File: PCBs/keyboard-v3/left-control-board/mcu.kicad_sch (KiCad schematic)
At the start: 5 parts, among them J301 F31Z1A7H111008, U301 STM32G0C1CEUx

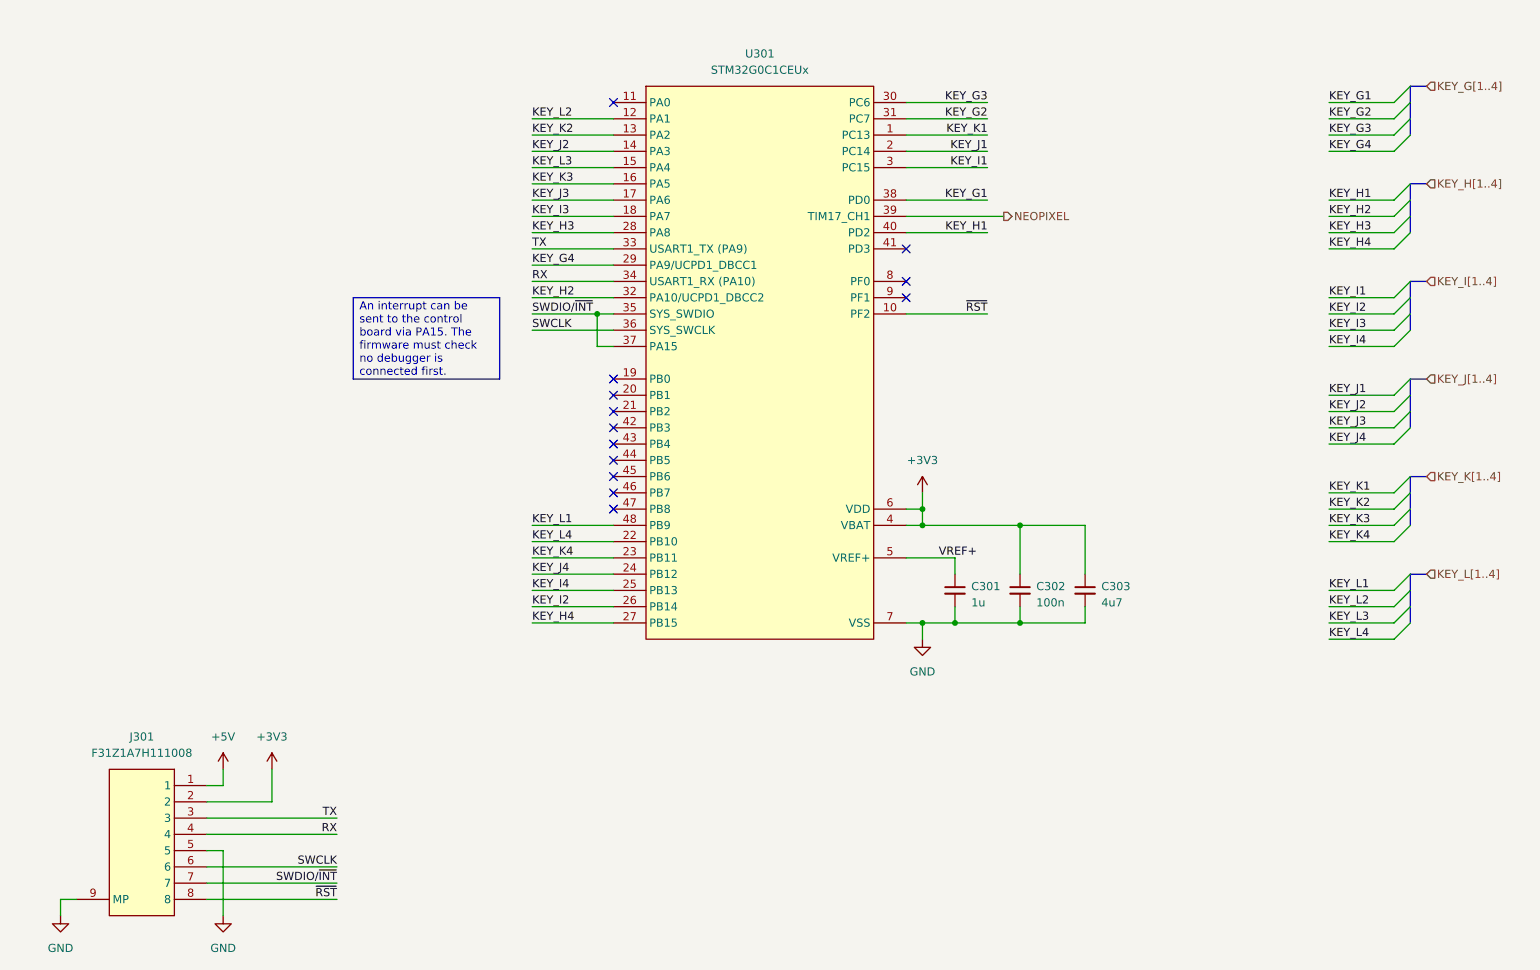
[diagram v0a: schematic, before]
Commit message: Added debug-breakout board, progress on right side schematics & layout
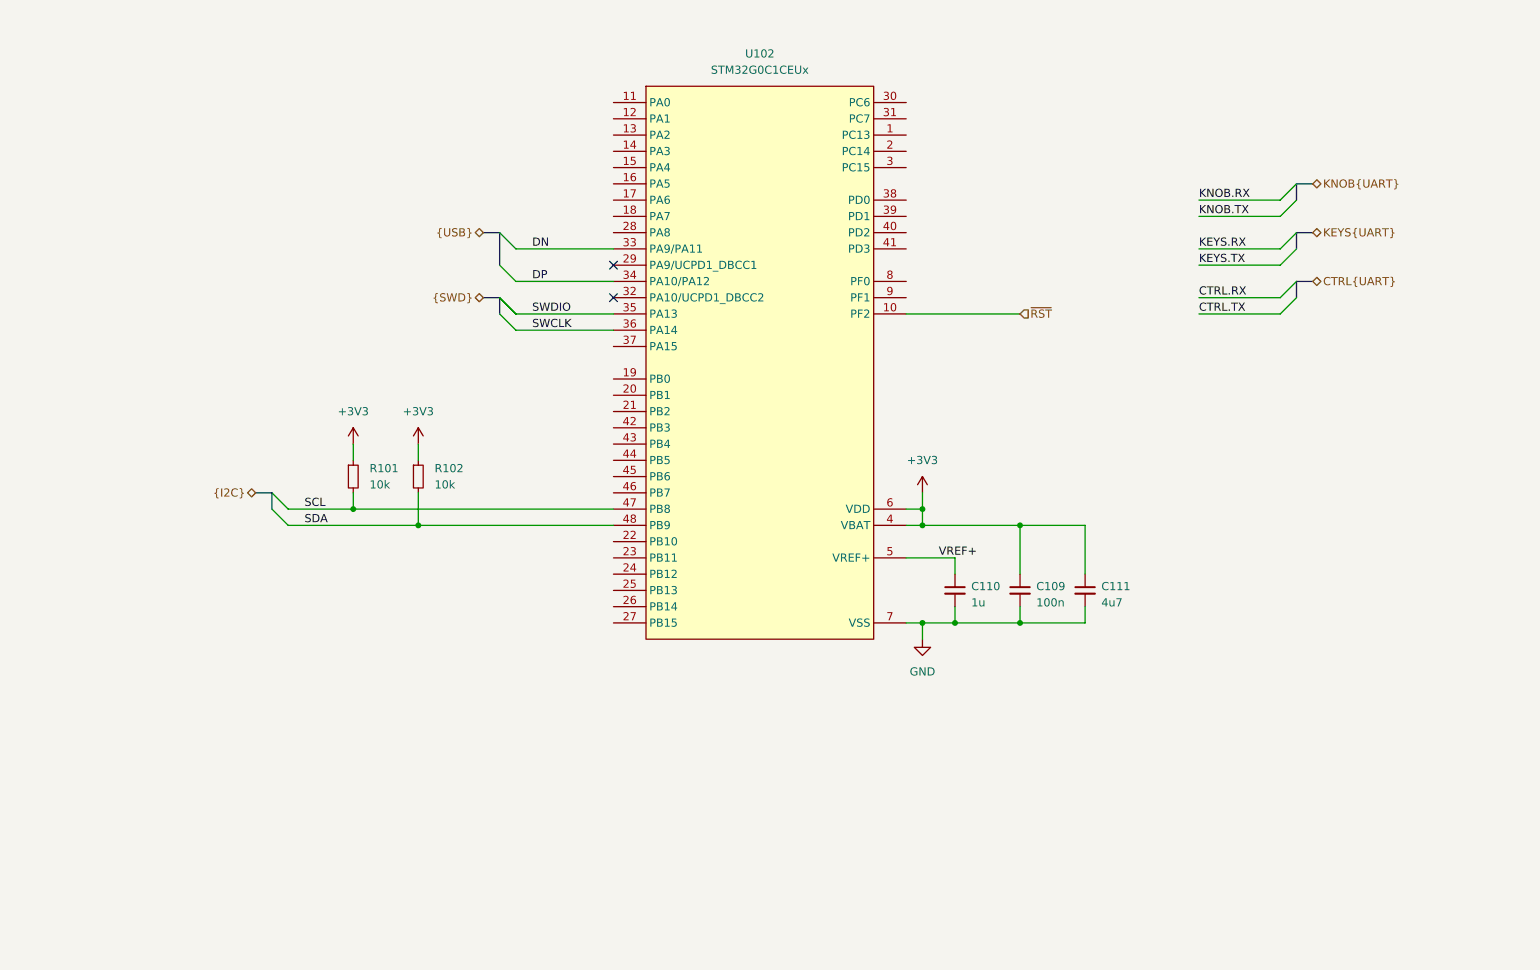
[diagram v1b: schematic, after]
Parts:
- removed J301: F31Z1A7H111008, project_footprints:F31Z1A7H111008, symbol CONN-FPC:F31Z-1A7H1-11008
- added R101, R102: 10k, project_footprints:R_0402, symbol DEV:R_SMALL
- renumbered C302 to C109, C301 to C110, C303 to C111, U301 to U102
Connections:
- net +3V3: now also R101.1, R102.1
- net SCL: now reaches U102.47 (PB8)
- net SCL: now also R101.2
- net KEY_G1: no longer names the net of U102.38 (PD0)
- net KEY_G2: no longer names the net of U102.31 (PC7)
- net KEY_G3: no longer names the net of U102.30 (PC6)
- net KEY_G4: no longer names the net of U102.29 (PA9/UCPD1_DBCC1)
- net KEY_H1: no longer names the net of U102.40 (PD2)
- net KEY_H2: no longer names the net of U102.32 (PA10/UCPD1_DBCC2)
- net KEY_H3: no longer names the net of U102.28 (PA8)
- net KEY_H4: no longer names the net of U102.27 (PB15)
- net KEY_I1: no longer names the net of U102.3 (PC15)
- net KEY_I2: no longer names the net of U102.26 (PB14)
- net KEY_I3: no longer names the net of U102.18 (PA7)
- net KEY_I4: no longer names the net of U102.25 (PB13)
- net KEY_J1: no longer names the net of U102.2 (PC14)
- net KEY_J2: no longer names the net of U102.14 (PA3)
- net KEY_J3: no longer names the net of U102.17 (PA6)
- net KEY_J4: no longer names the net of U102.24 (PB12)
- net KEY_K1: no longer names the net of U102.1 (PC13)
- net KEY_K2: no longer names the net of U102.13 (PA2)
- net KEY_K3: no longer names the net of U102.16 (PA5)
- net KEY_K4: no longer names the net of U102.23 (PB11)
- net KEY_L1 renamed SDA
- net SDA: now also R102.2
- net KEY_L2: no longer names the net of U102.12 (PA1)
- net KEY_L3: no longer names the net of U102.15 (PA4)
- net KEY_L4: no longer names the net of U102.22 (PB10)
- net NEOPIXEL: no longer names the net of U102.39 (PD1)
- net RX renamed DP
- net SWDIO/~{INT}: no longer names the net of U102.37 (PA15)
- net SWDIO/~{INT}: no longer U102.35 (PA13)
- net TX renamed DN
- new net SWDIO: U102.35 (PA13)
- no-connect marks 13 -> 2

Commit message: Left knob board done
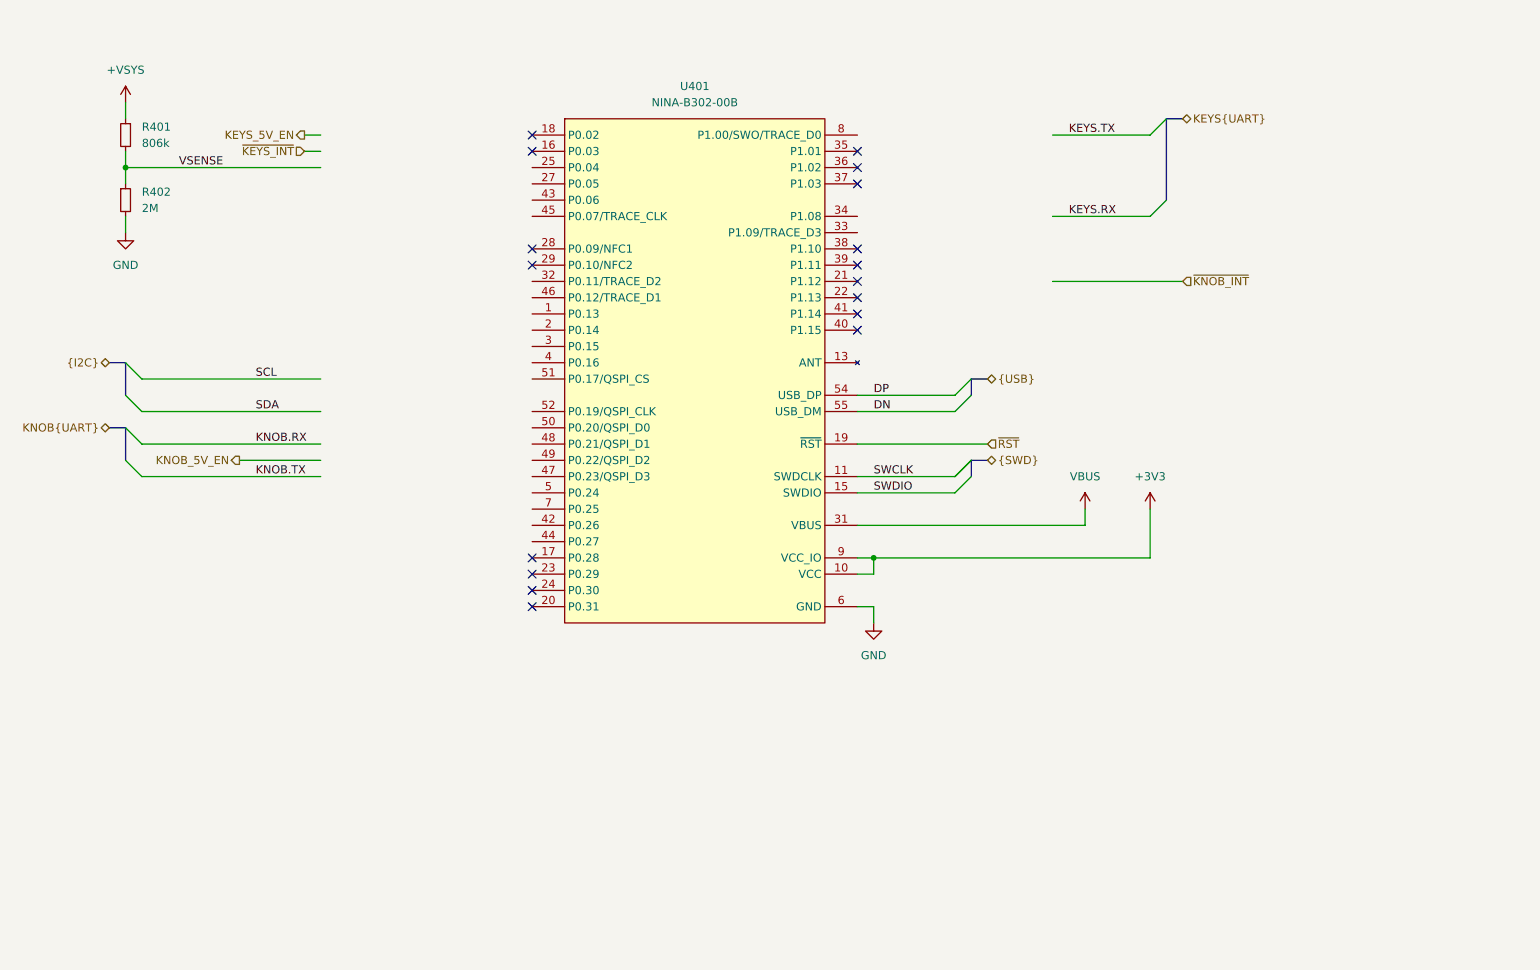
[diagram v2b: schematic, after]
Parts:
- removed C109: 100n, project_footprints:C_0402, symbol DEV:C_SMALL
- removed C110: 1u, project_footprints:C_0402, symbol DEV:C_SMALL
- removed C111: 4u7, project_footprints:C_0402, symbol DEV:C_SMALL
- removed R101, R102: 10k, project_footprints:R_0402, symbol DEV:R_SMALL
- removed U102: STM32G0C1CEUx, project_footprints:QFN50P700X700X60-49N-D, symbol STM32:STM32G0C1CEUx
- added R401: 806k, project_footprints:R_0402, symbol DEV:R_SMALL
- added R402: 2M, project_footprints:R_0402, symbol DEV:R_SMALL
- added U401: NINA-B302-00B, project_footprints:NINAB30200B, symbol NRF:NINA-B302-00B
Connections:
- net +3V3: now also U401.10 (VCC), U401.9 (VCC_IO)
- net DN: now also U401.55 (USB_DM)
- net DP: now also U401.54 (USB_DP)
- net GND: now also R402.2, U401.12 (GND), U401.14 (GND), U401.26 (GND), U401.30 (GND), U401.53 (GND), U401.56 (GND), U401.57 (GND), U401.58 (GND), U401.59 (GND), U401.6 (GND), U401.60 (GND), U401.61 (GND), U401.62 (GND), U401.63 (GND), U401.64 (GND), U401.65 (GND), U401.66 (GND), U401.67 (GND)
- net SWCLK: now also U401.11 (SWDCLK)
- net SWDIO: now also U401.15 (SWDIO)
- net ~{RST}: now also U401.19 (~{RST})
- new net +VSYS: R401.1
- new net VBUS: U401.31 (VBUS)
- new net VSENSE: R401.2, R402.1
- no-connect marks 2 -> 17

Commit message: Left control board done
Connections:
- net KEYS.RX: now also U401.8 (P1.00/SWO/TRACE_D0)
- net KEYS.TX: now also U401.7 (P0.25)
- net KEYS_5V_EN: now also U401.4 (P0.16)
- net KNOB.RX: now also U401.3 (P0.15)
- net KNOB.TX: now also U401.2 (P0.14)
- net KNOB_5V_EN: now also U401.52 (P0.19/QSPI_CLK)
- net SCL: now also U401.50 (P0.20/QSPI_D0)
- net SDA: now also U401.51 (P0.17/QSPI_CS)
- net VSENSE: now also U401.25 (P0.04)
- net ~{KEYS_INT}: now also U401.5 (P0.24)
- net ~{KNOB_INT}: now also U401.1 (P0.13)
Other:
- moved on the sheet: R401, R402
